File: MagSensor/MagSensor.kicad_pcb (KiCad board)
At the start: 4 copper layers, 115 x 101.6 mm, 176 parts, among them P1 009155004541006, P2 USB_Micro B, P3 PGM_DBG, P4 ER-CON2.0-2P-SMD, P5 CONN_01X03, P6 POGO_PGM, P7 SFV30R-4STBE1HLF, Q1 MMBT2222, Q2 BCW89, Q3 BCW89, Q4 MMBT2222, Q5 MMBT2222, Q6 MMBT2222, Q7 MMBT2222, Q8 MMBT2222, U1 AT25_EEPROM, U10 SiP32510, U11 A4953, U12 SiP32510, U13 MCP4012T-503E/CH, U16 PiezoTransducer, U19 TLV493D, U2 TCR2EE/EF, U20 TLV493D, U21 TLV493D, U22 TLV493D, U3 SiP32510, U4 SiP32510, U5 MCP73831-2AC, U6 XMC4200-F64, U7 SiP32510, U8 SiP32510, U9 LSM6DS3, Y1 12MHz

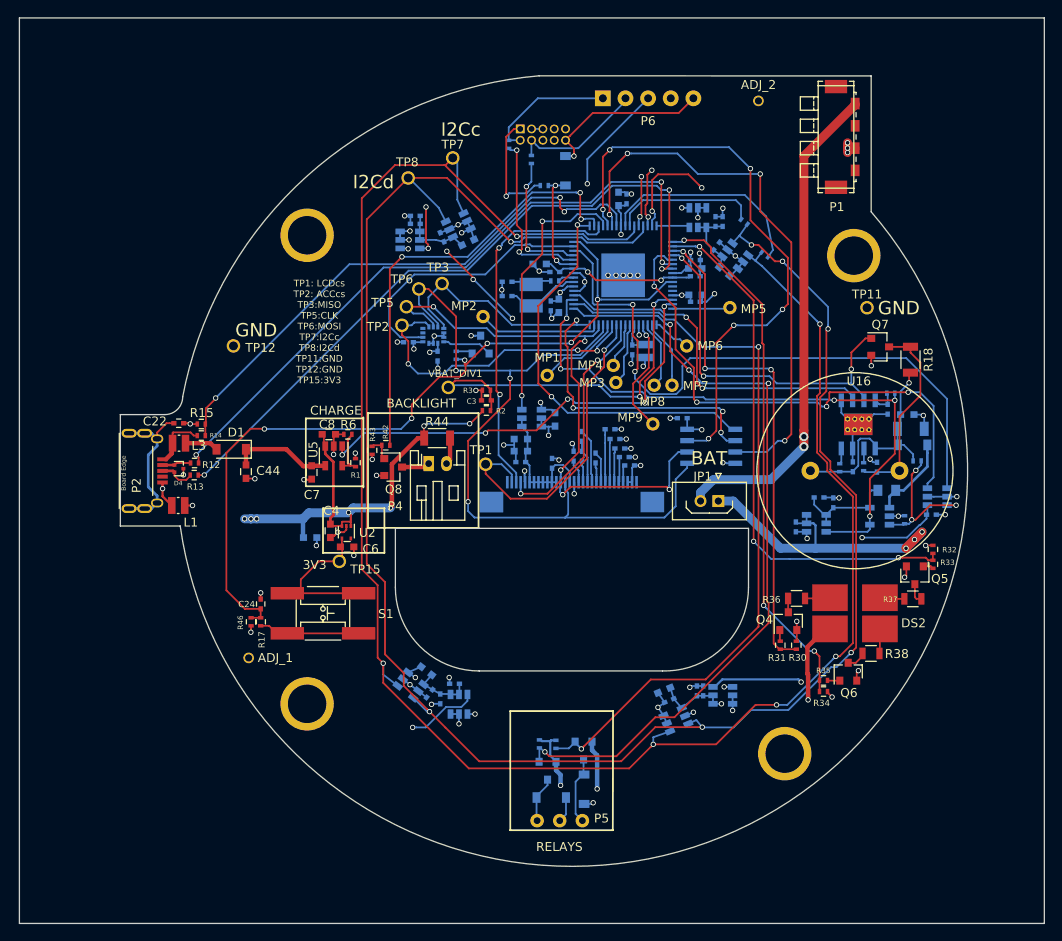
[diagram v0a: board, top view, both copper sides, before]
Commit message: Six sensor system DRC and ERC completed
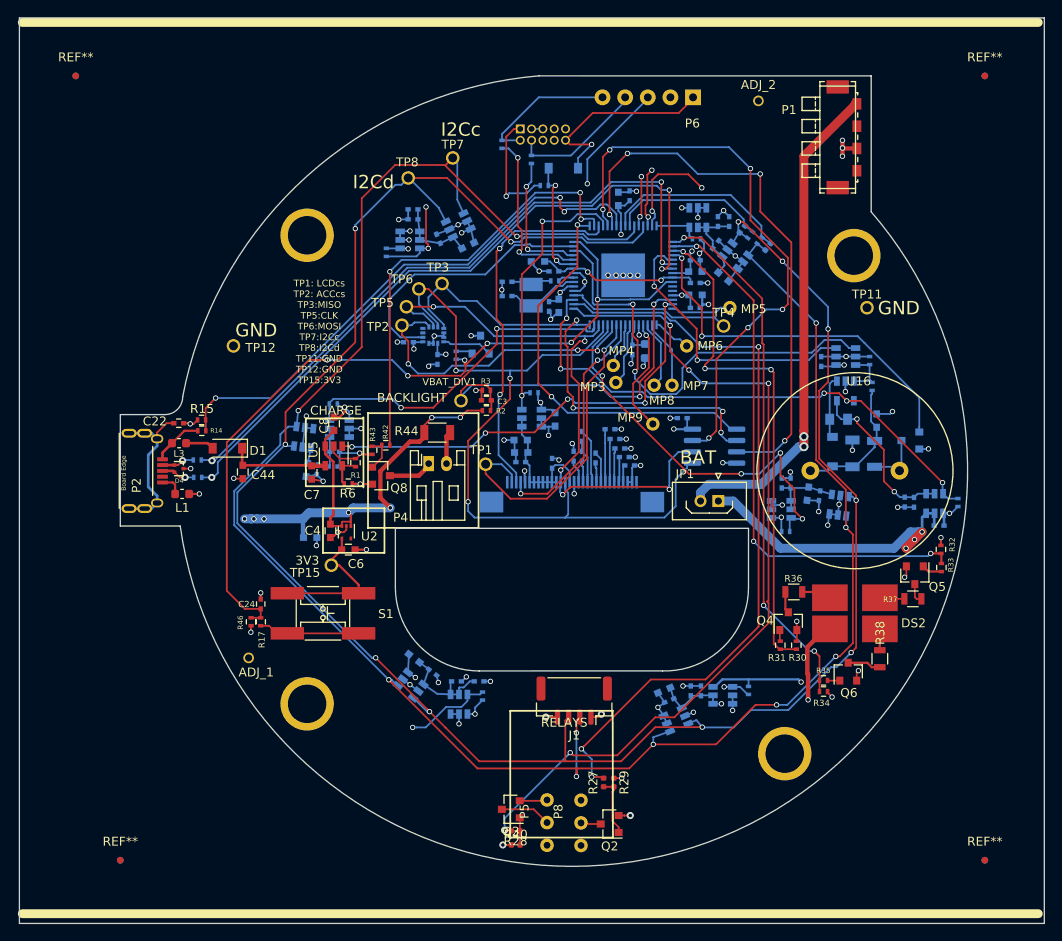
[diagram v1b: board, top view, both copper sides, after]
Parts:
- removed D7, D8: MBR0520LT1G, Diodes_SMD:D_SOD-123
- removed MP1, MP2: TEST, Measurement_Points:Measurement_Point_Round-TH_Small
- removed R72, R73: 10K, Resistors_SMD:R_0402
- added C52: 0.1uF, Capacitors_SMD:C_0402, B.Cu at (150.5, 128.4)
- added C53: 1uF, Capacitors_SMD:C_0402, B.Cu at (100.2, 126.5)
- added C63: 4.7uF, Capacitors_SMD:C_0603, B.Cu at (153.5, 129.6)
- added C64: 0.1uF, Capacitors_SMD:C_0402, B.Cu at (98.4, 126.9)
- added C65: 0.1uF, Capacitors_SMD:C_0402, B.Cu at (154.8, 129.8)
- added J1: Conn_01x04, Connector_JST:JST_GH_SM04B-GHS-TB_1x04-1MP_P1.25mm_Horizontal, F.Cu at (127.3, 152.8)
- added P8: CONN_01X03, SamLib:3_50D_100SP_Solder, F.Cu at (128.0, 166.5)
- added R21: 390K (1%), Resistors_SMD:R_0402, B.Cu at (117.0, 152.3)
- added R22: 390K (1%), Resistors_SMD:R_0402, B.Cu at (141.0, 101.0)
- added R24: 390K (1%), Resistors_SMD:R_0402, B.Cu at (170.3, 130.6)
- added R25: 390K (1%), Resistors_SMD:R_0402, B.Cu at (100.2, 119.5)
- added R26: 390K (1%), Resistors_SMD:R_0402, B.Cu at (151.0, 133.8)
- added R27: 10K, Resistor_SMD:R_0402_1005Metric, F.Cu at (130.6, 162.0)
- added R28: 10K, Resistor_SMD:R_0402_1005Metric, F.Cu at (120.7, 167.4)
- added R29: 10K, Resistor_SMD:R_0402_1005Metric, F.Cu at (131.7, 162.0)
- added R40: 10K, Resistor_SMD:R_0402_1005Metric, F.Cu at (120.7, 169.0)
- added R41: 4.7K, Resistor_SMD:R_0402_1005Metric, B.Cu at (146.1, 99.9)
- added R45: 4.7K, Resistor_SMD:R_0402_1005Metric, B.Cu at (149.0, 101.9)
- added REF**: Fiducial_0.75mm_Mask2.25mm, Fiducial:Fiducial_0.75mm_Mask2.25mm, B.Cu at (173.3, 170.7)
- added REF**: Fiducial_0.75mm_Mask2.25mm, Fiducial:Fiducial_0.75mm_Mask2.25mm, F.Cu at (173.3, 170.7)
- added REF**: Fiducial_0.75mm_Mask2.25mm, Fiducial:Fiducial_0.75mm_Mask2.25mm, B.Cu at (76.3, 170.7)
- added REF**: Fiducial_0.75mm_Mask2.25mm, Fiducial:Fiducial_0.75mm_Mask2.25mm, F.Cu at (76.3, 170.7)
- added REF**: Fiducial_0.75mm_Mask2.25mm, Fiducial:Fiducial_0.75mm_Mask2.25mm, B.Cu at (173.3, 82.7)
- added REF**: Fiducial_0.75mm_Mask2.25mm, Fiducial:Fiducial_0.75mm_Mask2.25mm, B.Cu at (71.3, 82.7)
- added REF**: Fiducial_0.75mm_Mask2.25mm, Fiducial:Fiducial_0.75mm_Mask2.25mm, F.Cu at (71.3, 82.7)
- added REF**: Fiducial_0.75mm_Mask2.25mm, Fiducial:Fiducial_0.75mm_Mask2.25mm, F.Cu at (173.3, 82.7)
- added TP4: SPICLK, SamLib:TP_Pin40, F.Cu at (144.0, 110.8)
- added U14: SiP32510, TO_SOT_Packages_SMD:SOT-23-6, B.Cu at (150.5, 131.3)
- added U15: TLV493D, TO_SOT_Packages_SMD:SOT-23-6, B.Cu at (96.9, 123.3)
- added U17: TLV493D, TO_SOT_Packages_SMD:SOT-23-6, B.Cu at (157.0, 130.9)
- C55: value 0.1uF (50V) DNS -> 1uF
- C56: value 0.1uF (50V) DNS -> 4.7uF; footprint Capacitors_SMD:C_0402 -> Capacitors_SMD:C_0603
- L1, L2, L3: footprint Inductors:Inductor_Wurth_MAPI-2010 -> Inductor_SMD:L_0603_1608Metric
- Q2, Q3: value BCW89 -> MMBT2222; footprint TO_SOT_Packages_SMD:SOT-23 -> Package_TO_SOT_SMD:SOT-23; moved to F.Cu
- Q7, R12, R13, R18: moved to B.Cu
- R19, R20, R7: value 4.7K -> 390K (1%)
- U1: value AT25_EEPROM -> AT25xxx; footprint Housings_SOIC:SOIC-8_3.9x4.9mm_Pitch1.27mm -> Package_SO:SOIC-8_3.9x4.9mm_P1.27mm
- U11: value A4953 -> SiP32510; footprint Housings_SOIC:HTSOP-8-1EP_3.9x4.9mm_Pitch1.27mm_ThermalVias -> TO_SOT_Packages_SMD:SOT-23-6
- moved C47 62.2 mm to (100.4, 124.9), turned to 0 degrees
- moved C56 61.3 mm to (97.3, 126.9), turned to 262.8 degrees
- moved U11 58.2 mm to (100.9, 122.3), turned to 0 degrees
- moved R19 56.3 mm to (106.2, 102.5), turned to 90 degrees
- moved R7 40.0 mm to (122.7, 118.3), turned to 0 degrees
- moved R20 28.2 mm to (146.8, 151.7), turned to 270 degrees
- moved C48 21.2 mm to (155.0, 114.7), turned to 90 degrees
- moved U13 18.8 mm to (157.7, 114.2)
- moved R9 18.3 mm to (160.4, 114.6)
- moved C66 16.1 mm to (168.2, 133.2), turned to 0 degrees
- moved G1 14.6 mm to (157.7, 118.1), turned to 270 degrees
- moved U10 13.5 mm to (167.7, 130.7), turned to 270 degrees
- moved R18 11.3 mm to (161.0, 125.1), turned to 270 degrees
- moved Q7 11.0 mm to (165.0, 123.6), turned to 180 degrees
- moved P6 10.1 mm to (140.6, 85.1), turned to 180 degrees
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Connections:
- net /LCD/~LCD_BACKLIGHT renamed /LCD/LCD_BACKLIGHT
- C47 pad 1: GND -> /Sensors and Interfaces/PowerMagSenseM1
- C47 pad 2: Net-(C47-Pad2) -> GND
- C55 pad 1: GND -> /Sensors and Interfaces/PowerMagSenseM2
- C55 pad 2: Net-(C55-Pad2) -> GND
- C56 pad 1: GND -> /Sensors and Interfaces/PowerMagSenseM1
- C56 pad 2: /Piezo/V_Piezo -> GND
- P5 pad 1: Net-(D7-Pad1) -> (no net)
- P5 pad 2: GND -> Net-(P5-Pad2)
- P5 pad 3: Net-(D8-Pad1) -> GND
- P6 pad 1: Net-(P3-Pad2) -> Net-(D5-Pad1)
- P6 pad 2: Net-(P3-Pad4) -> GND
- P6 pad 4: GND -> Net-(P3-Pad4)
- P6 pad 5: Net-(D5-Pad1) -> Net-(P3-Pad2)
- Q2 pad 1: /Sensors and Interfaces/~Relay1 -> Net-(Q2-Pad1)
- Q2 pad 2: +BATT -> GND
- Q2 pad 3: Net-(D7-Pad1) -> Net-(P8-Pad2)
- Q3 pad 1: /Sensors and Interfaces/~Relay2 -> Net-(Q3-Pad1)
- Q3 pad 2: +BATT -> GND
- Q3 pad 3: Net-(D8-Pad1) -> Net-(P5-Pad2)
- Q7 pad 3: Net-(C55-Pad2) -> Net-(Q7-Pad3)
- R18 pad 2: Net-(C55-Pad2) -> Net-(Q7-Pad3)
- R19 pad 1: Net-(R19-Pad1) -> /Sensors and Interfaces/S_PWR1_EN
- R19 pad 2: /Piezo/V_Piezo -> GND
- R20 pad 1: Net-(C55-Pad2) -> /Sensors and Interfaces/S_PWR3_EN
- R20 pad 2: Net-(R20-Pad2) -> GND
- R7 pad 1: /Piezo/PZ_EN -> /LCD/LCD_EN
- R7 pad 2: Net-(C47-Pad2) -> GND
- U11 pad 1: GND -> /Sensors and Interfaces/PowerMagSenseM1
- U11 pad 2: /Piezo/~PZ -> /Sensors and Interfaces/PowerMagSenseM1
- U11 pad 3: /Piezo/PZ -> /Sensors and Interfaces/S_PWR_M1_EN
- U11 pad 4: Net-(C47-Pad2) -> GND
- U11 pad 5: /Piezo/V_Piezo -> +3V3
- U11 pad 6: Net-(R20-Pad2) -> +3V3
- U16 pad 2: Net-(C55-Pad2) -> Net-(Q7-Pad3)
- U6 pad 28: Net-(MP1-Pad1) -> /Sensors and Interfaces/S_PWR_M2_EN
- U6 pad 31: Net-(MP2-Pad1) -> /Sensors and Interfaces/S_PWR_M1_EN
- U6 pad 33: /Sensors and Interfaces/~Relay2 -> /Sensors and Interfaces/Relay2
- U6 pad 34: /Sensors and Interfaces/~Relay1 -> /Sensors and Interfaces/Relay1
- U6 pad 36: /Piezo/~PZ -> Net-(TP4-Pad1)
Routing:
- net /Sensors and Interfaces/Relay2: track 0.00 -> 95.3 mm, vias 0 -> 5
- net /Sensors and Interfaces/~Relay2: track 88.0 -> 0.00 mm, vias 4 -> 0
- net /Sensors and Interfaces/Relay1: track 0.00 -> 84.7 mm, vias 0 -> 3
- net /Sensors and Interfaces/~Relay1: track 83.2 -> 0.00 mm, vias 2 -> 0
- net /Sensors and Interfaces/S_PWR_M2_EN: track 0.00 -> 44.6 mm, vias 0 -> 4
- net GND: track 131.5 -> 173.1 mm, vias 78 -> 87
- net /Piezo/~PZ: track 40.1 -> 0.00 mm, vias 2 -> 0
- net /Sensors and Interfaces/S_PWR_M1_EN: track 0.00 -> 38.1 mm, vias 0 -> 2
- net /Piezo/vPU~D: track 58.7 -> 31.8 mm, vias 4 -> 2
- net Net-(C55-Pad2): track 22.1 -> 0.00 mm
- net /Sensors and Interfaces/I2C_0_DTA: track 218.6 -> 240.3 mm, vias 7 -> 11
- net /Piezo/~vPCS: track 71.2 -> 50.1 mm
- net /Sensors and Interfaces/I2C_0_CLK: track 218.6 -> 238.6 mm, vias 6 -> 10
- net Net-(TP4-Pad1): track 0.00 -> 18.3 mm
- net Net-(MP2-Pad1): track 13.8 -> 0.00 mm
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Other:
- board text added: "MSm1"
- board text added: "MSm2"
- board text added: "TP1: LCDcs TP2:ACCcs TP3:MISO TP5:CLK TP6:MOSI TP7:I2Cc TP8: I2Cd TP11:GND TP12:GND TP15:3V3"
- board text removed: "1"
- board text removed: "2"
- board text removed: "G"
- board text removed: "TP1: LCDcs TP2:ACCcs TP3:MISO TP5:CLK TP6:MOSI TP7:I2Cc TP8:I2Cd TP11:GND TP12:GND TP15:3V3"
